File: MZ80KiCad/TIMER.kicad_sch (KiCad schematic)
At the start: 17 parts, among them U1 ICM7555xP, U11 74LS126, U12 74LS74, U18 8253, U23 74LS02, U3 7406

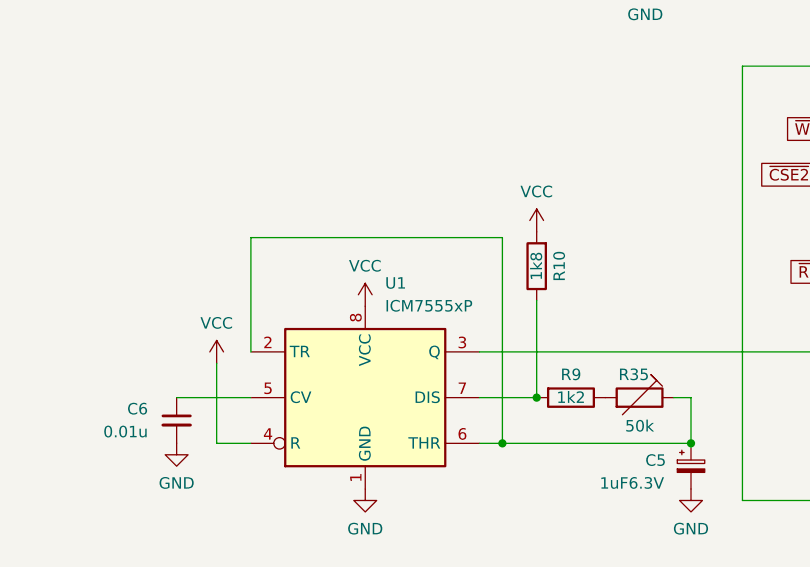
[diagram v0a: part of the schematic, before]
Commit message: fix U47 pin18 pin19
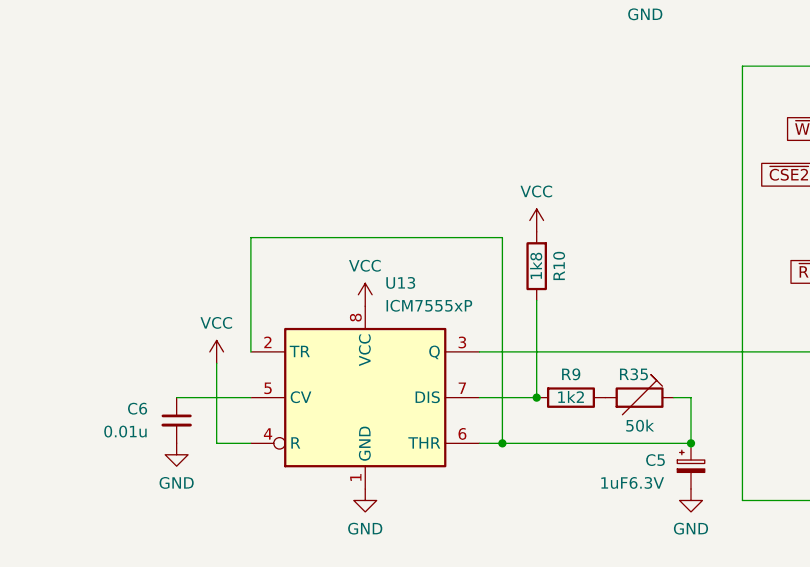
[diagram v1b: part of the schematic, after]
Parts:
- renumbered U1 to U13
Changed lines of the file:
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@@
   (symbol (lib_id "Timer:ICM7555xP") (at 104.775 130.81 0) (unit 1)
     (in_bom yes) (on_board yes) (dnp no) (fields_autoplaced)
-    (property "Reference" "U1" (at 106.9691 118.11 0)
+    (property "Reference" "U13" (at 106.9691 118.11 0)
       (effects (font (size 1.27 1.27)) (justify left))
     )
@@
     (instances
       (project "MZ80"
-        (path "/4c07815a-c510-44da-af98-4d055fa8c080/7b3a55ce-66ff-4227-8a4d-d2f73cb0a8bf"
-          (reference "U1") (unit 1)
-        )
         (path "/4c07815a-c510-44da-af98-4d055fa8c080/acc3a0ed-c820-4ad2-a14a-1c59b599576b"
           (reference "U13") (unit 1)
